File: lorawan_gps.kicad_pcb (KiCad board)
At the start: 2 copper layers, 95 x 20 mm, 120 parts, among them IC1 TPS61201, J1 MICRO-USB, P1 BL_PAD, P11 CONN_01X04, P2 SWD_DAT, P3 SWD_CLK, P4 SWD_3V3, P5 SWD_GND, P6 SWD_RST, Q1 Q_PMOS_GSD, SW1 SW_PUSH, SW2 SW_PUSH, U1 SHT21, U2 MPU-9250, U3 RFM9xW, U4 SAMD21E17A, U5 MAX-M8, Y1 32.768kHz

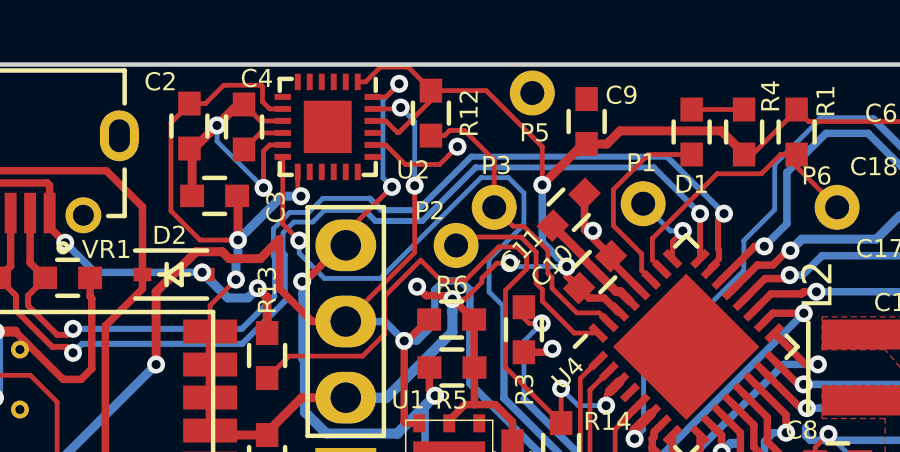
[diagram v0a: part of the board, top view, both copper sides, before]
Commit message: Fixed track near edge by accelerometer
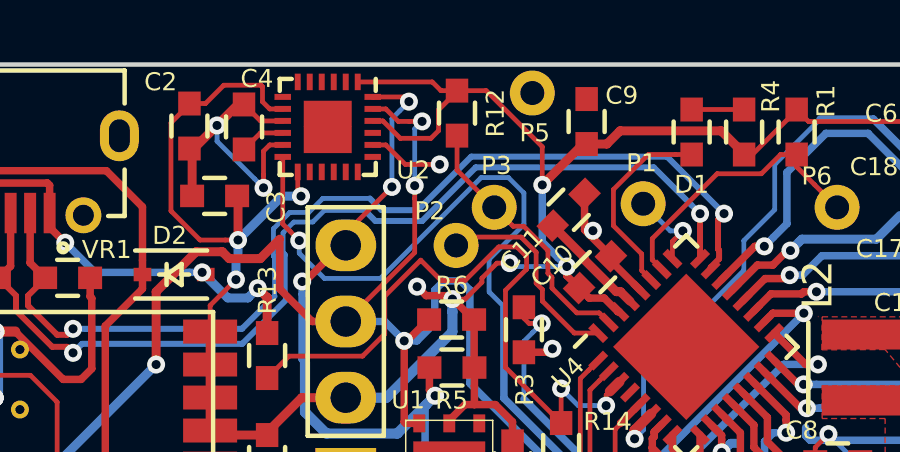
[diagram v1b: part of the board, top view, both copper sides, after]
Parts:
- moved R12 0.87 mm to (130.4, 71.6)
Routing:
- net Net-(P3-Pad1): track 10.6 -> 9.37 mm
- net GND: track 223.0 -> 222.1 mm
- net +3V3: track 157.1 -> 157.9 mm
